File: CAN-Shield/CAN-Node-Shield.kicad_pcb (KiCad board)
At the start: 2 copper layers, 59.6 x 55.3 mm, 22 parts, among them J1 Main_Port_1, J10 IOH, J2 Main_Port_2, J3 Sensor, J4 Sensor, J5 Sensor, J6 Sensor, J7 Power, J8 Analog, J9 IOL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

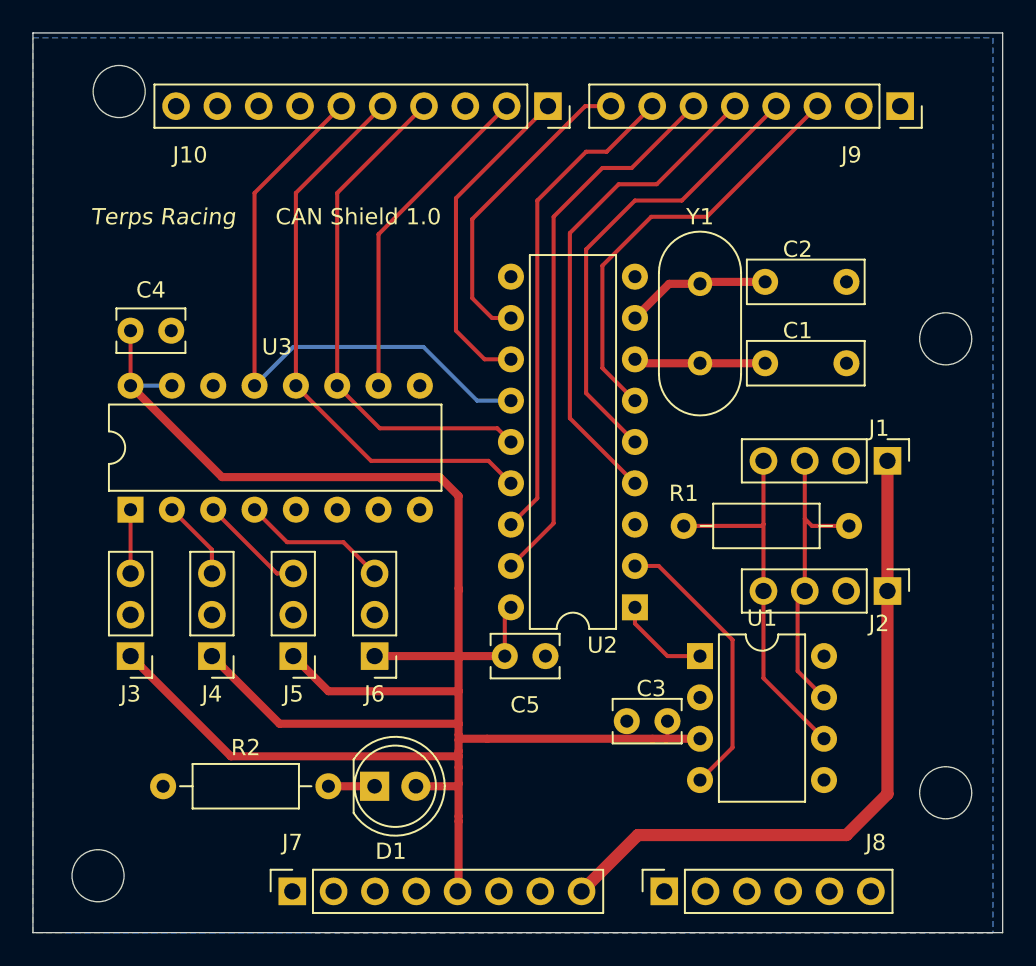
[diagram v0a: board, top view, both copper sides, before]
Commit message: CAN terminating resistor change
I updated the layout to include options for both High-speed CAN and Low-speed CAN terminating resistor configurations. There are positions for either type of termination so the board can be used for either bus type.
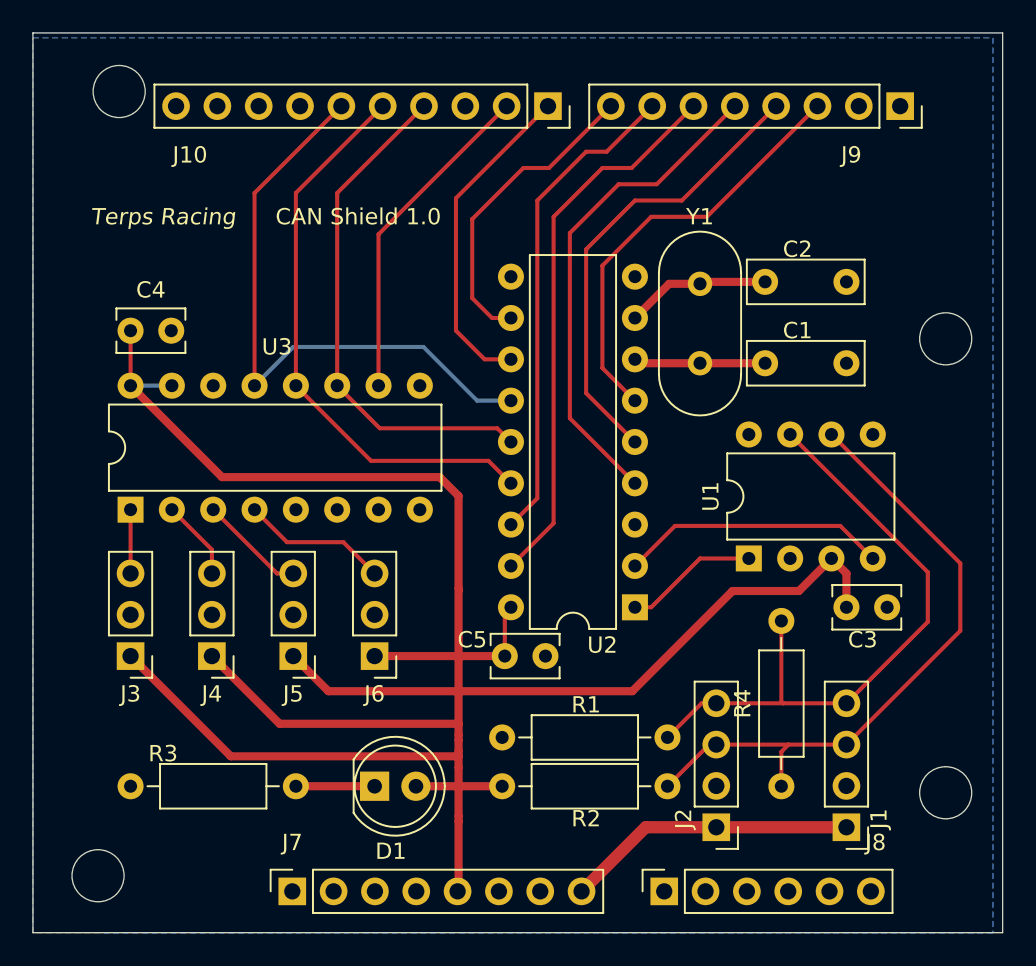
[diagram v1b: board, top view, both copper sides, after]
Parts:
- added R3: 120, Resistor_THT:R_Axial_DIN0207_L6.3mm_D2.5mm_P10.16mm_Horizontal, F.Cu at (118.0, 91.0)
- added R4: 120, Resistor_THT:R_Axial_DIN0207_L6.3mm_D2.5mm_P10.16mm_Horizontal, F.Cu at (158.0, 91.0)
- R1, R2: value 120 -> 500
- moved R2 31.0 mm to (151.0, 91.0), turned to 180 degrees
- moved J1 22.7 mm to (162.0, 93.5), turned to 180 degrees
- moved J2 17.9 mm to (154.0, 93.5), turned to 180 degrees
- moved C3 13.0 mm to (162.0, 80.0), turned to 0 degrees
- moved R1 13.0 mm to (151.0, 88.0), turned to 180 degrees
- moved U1 6.71 mm to (156.0, 77.0), turned to 90 degrees
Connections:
- R1 pad 2: Net-(J1-Pad3) -> GND
- R2 pad 1: GND -> Net-(J1-Pad3)
- R2 pad 2: Net-(D1-Pad1) -> +5V
- U1 pad 6: Net-(J1-Pad4) -> Net-(J1-Pad3)
- U1 pad 7: Net-(J1-Pad3) -> Net-(J1-Pad4)
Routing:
- net +12V: track 42.3 -> 18.4 mm
- net Net-(J1-Pad3): track 18.3 -> 40.0 mm
- net +5V: track 134.4 -> 151.0 mm
- net Net-(J1-Pad4): track 23.6 -> 39.2 mm
- net Net-(U1-Pad1): track 5.86 -> 8.27 mm
- net Net-(D1-Pad1): track 2.84 -> 4.84 mm
- net Net-(U1-Pad4): track 17.3 -> 16.5 mm

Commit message: Informational silkscreen and new board footprint
Changes made:
 - Adjusted bottom two Arduino headers; they were too far to the left by 2mm
 - Added silkscreen labels to header pins for easy identification of pin function
 - Reduced board footprint to allow for smaller enclosures
 - Chamfered corners to prevent them from being too pointy
 - Added my name :)
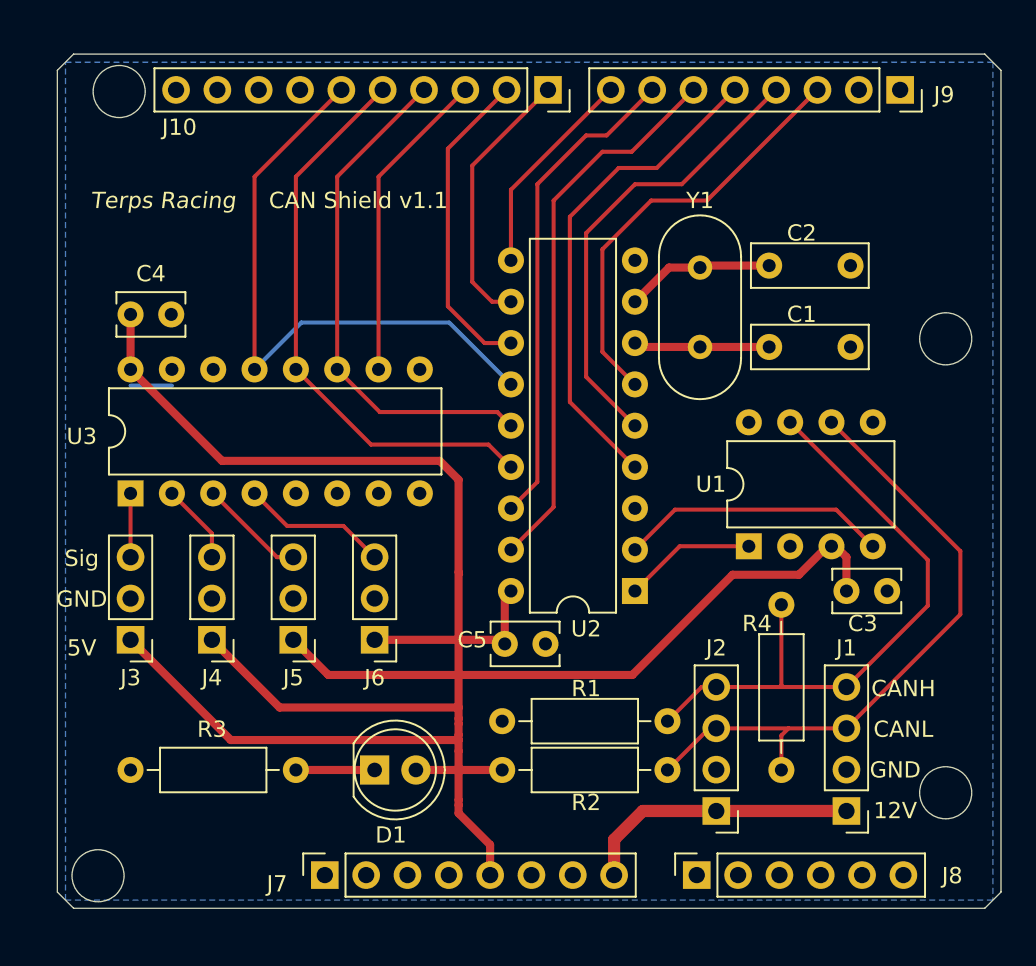
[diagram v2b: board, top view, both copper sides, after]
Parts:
- J1: value Main_Port_1 -> Main_Port
- J2: value Main_Port_2 -> Daisy-Chain-Port
- moved J7 2.24 mm to (129.9, 96.5)
- moved J8 2.24 mm to (152.8, 96.5)
- moved C1 1.03 mm to (162.2, 64.0)
- moved C2 1.03 mm to (162.2, 59.0)
- moved C3 1.00 mm to (162.0, 79.0)
- moved C4 1.00 mm to (118.0, 62.0)
- moved D1 1.00 mm to (133.0, 90.0)
- moved J1 1.00 mm to (162.0, 92.5)
- moved J10 1.00 mm to (143.7, 48.2)
- moved J2 1.00 mm to (154.0, 92.5)
- moved J3 1.00 mm to (118.0, 82.0)
- moved J4 1.00 mm to (123.0, 82.0)
- moved J5 1.00 mm to (128.0, 82.0)
- moved J6 1.00 mm to (133.0, 82.0)
- moved J9 1.00 mm to (165.3, 48.2)
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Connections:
- U2 pad 10: Net-(U2-Pad10) -> Net-(J9-Pad8)
- U2 pad 11: Net-(J9-Pad8) -> Net-(J10-Pad1)
- U2 pad 12: Net-(J10-Pad1) -> Net-(J10-Pad2)
- U3 pad 10: Net-(J10-Pad2) -> Net-(J10-Pad3)
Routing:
- net Net-(J10-Pad3): track 0.00 -> 19.4 mm
- net Net-(J9-Pad8): track 19.1 -> 13.0 mm
- net Net-(J10-Pad1): track 20.3 -> 16.6 mm
- net Net-(J10-Pad2): track 20.4 -> 19.6 mm
- net +5V: track 151.0 -> 151.8 mm
- net +12V: track 18.4 -> 17.7 mm
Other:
- board size 59.6 x 55.3 mm -> 58 x 52.5 mm
- board text added: "12V"
- board text added: "5V"
- board text added: "CAN Shield v1.1"
- board text added: "CANH"
- board text added: "CANL"
- board text added: "Designed By Derek Prestera"
- board text added: "GND"
- board text added: "Sig"
- board text removed: "CAN Shield 1.0"

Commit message: Alternated ADC inputs
Changes:
- Changed the ADC input ports to be connected to alternating ADC chip inputs to separate the traces to help reduce potential for cross-talk.
- Increased the width of the trace between the 12V power ports to allow for increased current capacity since this trace will carry power for all downstream devices.
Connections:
- U3 pad 2: Net-(J4-Pad3) -> GND
- U3 pad 3: Net-(J5-Pad3) -> Net-(J4-Pad3)
- U3 pad 4: Net-(J6-Pad3) -> GND
- U3 pad 5: GND -> Net-(J5-Pad3)
- U3 pad 7: GND -> Net-(J6-Pad3)
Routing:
- net Net-(J6-Pad3): track 9.00 -> 4.02 mm
- net Net-(J5-Pad3): track 6.54 -> 3.99 mm
- net Net-(J4-Pad3): track 4.94 -> 3.95 mm
